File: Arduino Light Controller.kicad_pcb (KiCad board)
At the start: 2 copper layers, 100 x 75 mm, 61 parts, among them J1 61300311121, J10 61300211121, J11 61300211121, J12 61300411121, J13 61300211121, J14 61300211121, J15 61300211121, J16 61300411121, J17 61300211121, J18 61300211121, J19 61300211121, J2 61300211121, J20 61300411121, J21 61300211121, J22 61300311121, J23 61300211121, J24 61300211121, J25 61300211121, J26 61300211121, J27 61300211121, J28 61300211121, J29 61300211121, J3 61300211121, J30 61300211121, J31 61300211121, J32 61300211121, J33 61300211121, J34 61300211121, J35 61300211121, J36 61300211121, J37 61300211121, J38 61300211121, J4 61300211121, J5 61300211121, J6 61300211121, J7 61300211121, J8 61300411121, J9 61300211121

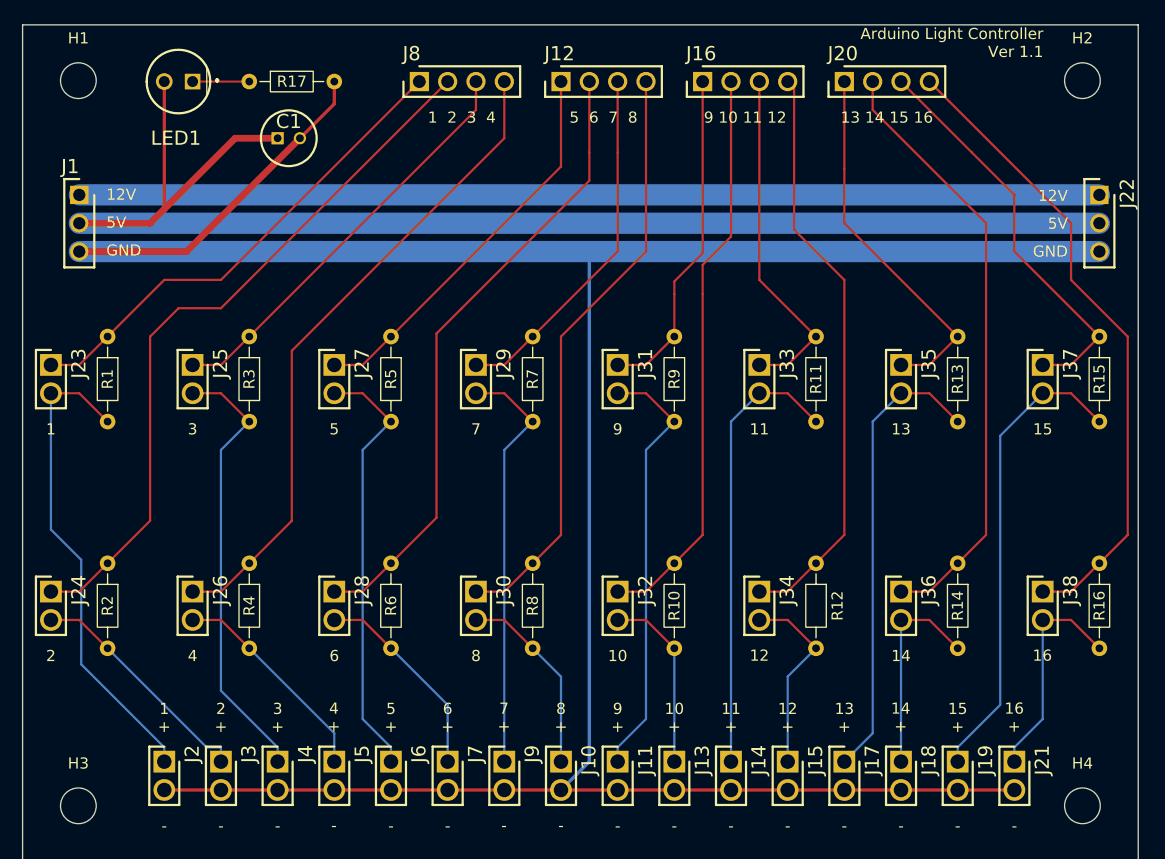
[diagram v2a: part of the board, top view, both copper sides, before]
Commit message: Updated components to the custom library and applied additional standards.
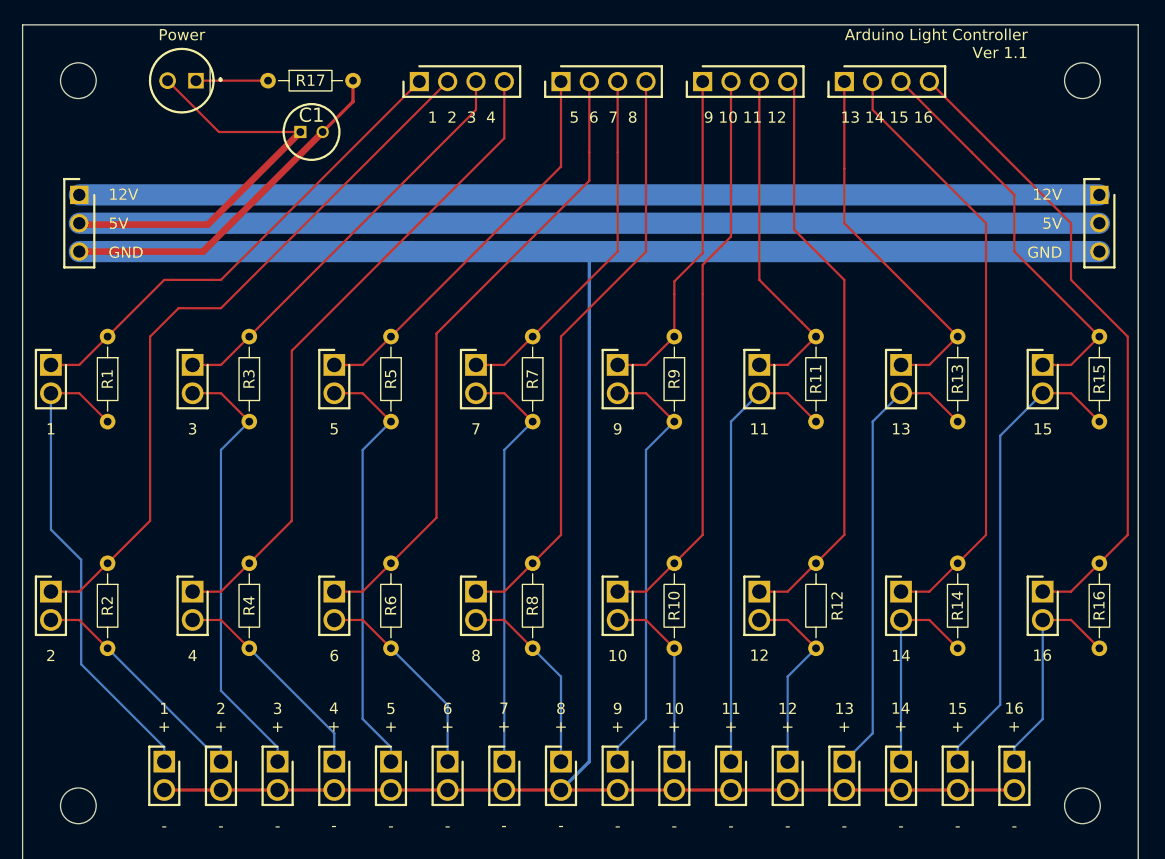
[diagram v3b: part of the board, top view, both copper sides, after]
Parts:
- moved C1 2.12 mm to (124.9, 59.6)
- moved R17 1.68 mm to (122.0, 55.0)
- moved LED1 0.31 mm to (115.5, 55.0)
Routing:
- net +5V: track 123.8 -> 128.6 mm
- net GND: track 247.3 -> 248.9 mm
- net Net-(LED1-K): track 5.08 -> 6.46 mm
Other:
- board text added: "Power"

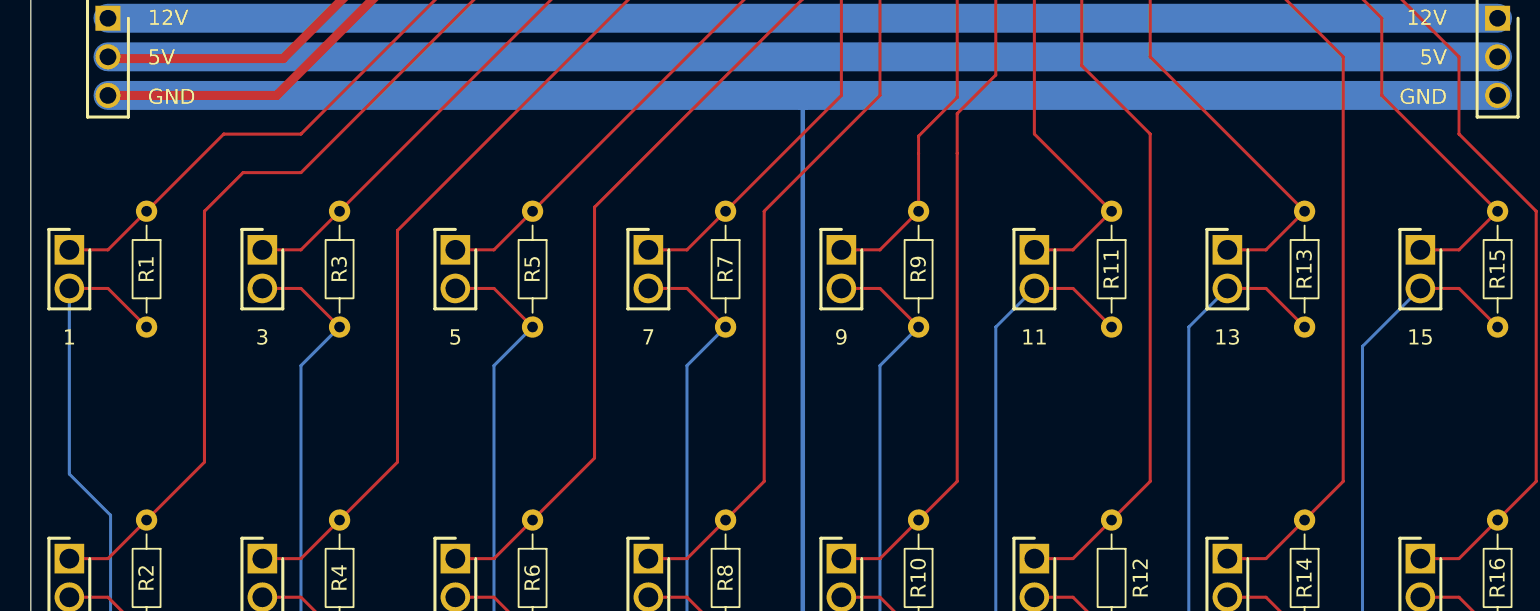
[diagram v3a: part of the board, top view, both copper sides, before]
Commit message: Added Resistor Bypass label to jumper pins.
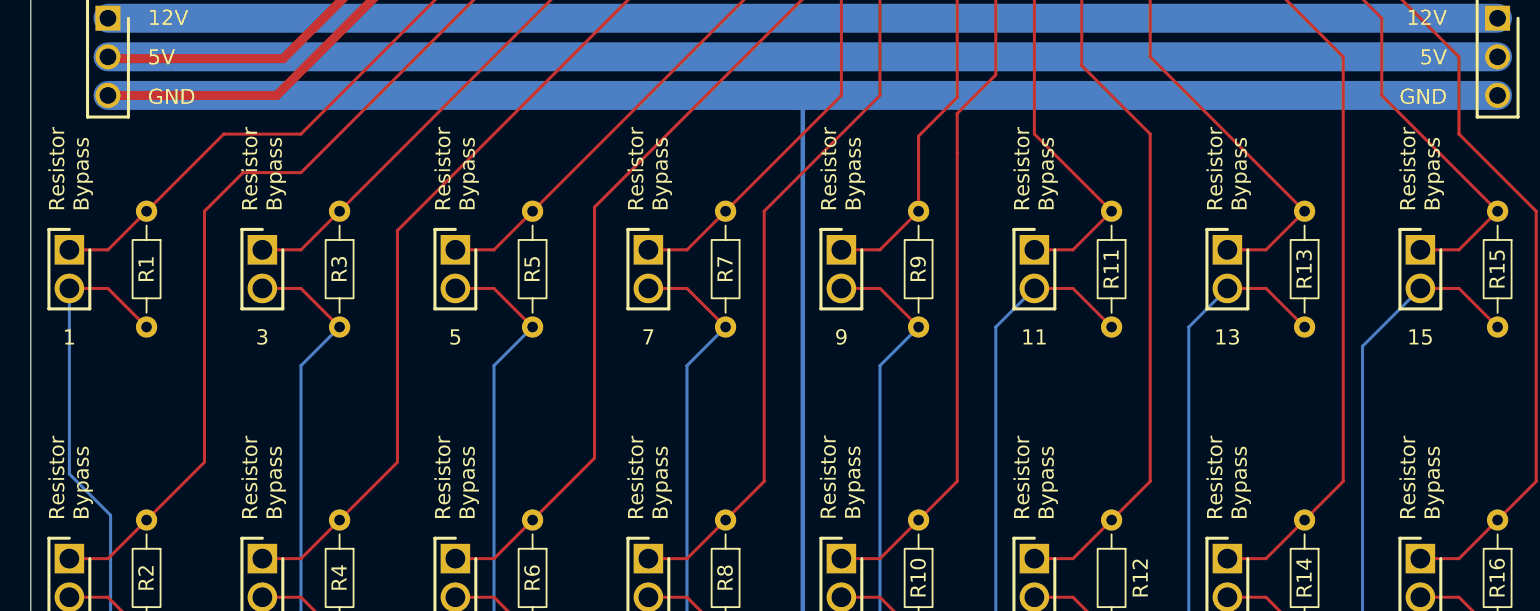
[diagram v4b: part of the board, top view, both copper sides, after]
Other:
- board text added: "Resistor Bypass"
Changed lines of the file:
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@@
+		)
+	)
+	(gr_text "Resistor\nBypass"
+		(at 178.74 77.94 90)
+		(layer "F.SilkS")
+		(effects
+			(font
+				(size 1 1)
+				(thickness 0.1)
+			)
+			(justify left)
 		)
 	)
@@
 		)
 	)
+	(gr_text "Resistor\nBypass"
+		(at 140.64 98.26 90)
+		(layer "F.SilkS")
+		(effects
+			(font
+				(size 1 1)
+				(thickness 0.1)
+			)
+			(justify left)
+		)
+	)
 	(gr_text "3\n+"
 		(at 122.86 113.5 0)
@@
 		)
 	)
+	(gr_text "Resistor\nBypass"
+		(at 115.24 77.94 90)
+		(layer "F.SilkS")
+		(effects
+			(font
+				(size 1 1)
+				(thickness 0.1)
+			)
+			(justify left)
+		)
+	)
 	(gr_text "6\n+"
 		(at 138.1 113.5 0)
@@
 		)
 	)
+	(gr_text "Resistor\nBypass"
+		(at 153.309206 98.243621 90)
+		(layer "F.SilkS")
+		(effects
+			(font
+				(size 1 1)
+				(thickness 0.1)
+			)
+			(justify left)
+		)
+	)
 	(gr_text "7\n+"
 		(at 143.150584 113.474628 0)
@@
 		)
 	)
+	(gr_text "Resistor\nBypass"
+		(at 191.44 77.94 90)
+		(layer "F.SilkS")
+		(effects
+			(font
+				(size 1 1)
+				(thickness 0.1)
+			)
+			(justify left)
+		)
+	)
 	(gr_text "7"
 		(at 140.64 86.83 0)
@@
 		)
 	)
+	(gr_text "Resistor\nBypass"
+		(at 153.34 77.94 90)
+		(layer "F.SilkS")
+		(effects
+			(font
+				(size 1 1)
+				(thickness 0.1)
+			)
+			(justify left)
+		)
+	)
 	(gr_text "11"
 		(at 166.04 86.83 0)
@@
 		)
 	)
+	(gr_text "Resistor\nBypass"
+		(at 178.74 98.26 90)
+		(layer "F.SilkS")
+		(effects
+			(font
+				(size 1 1)
+				(thickness 0.1)
+			)
+			(justify left)
+		)
+	)
+	(gr_text "Resistor\nBypass"
+		(at 102.54 77.94 90)
+		(layer "F.SilkS")
+		(effects
+			(font
+				(size 1 1)
+				(thickness 0.1)
+			)
+			(justify left)
+		)
+	)
+	(gr_text "Resistor\nBypass"
+		(at 127.94 77.94 90)
+		(layer "F.SilkS")
+		(effects
+			(font
+				(size 1 1)
+				(thickness 0.1)
+			)
+			(justify left)
+		)
+	)
 	(gr_text "4\n+"
 		(at 127.905646 113.474628 0)
@@
 		)
 	)
+	(gr_text "Resistor\nBypass"
+		(at 166.04 98.26 90)
+		(layer "F.SilkS")
+		(effects
+			(font
+				(size 1 1)
+				(thickness 0.1)
+			)
+			(justify left)
+		)
+	)
 	(gr_text "12V"
 		(at 193.2 65.8 0)
@@
 		)
 	)
+	(gr_text "Resistor\nBypass"
+		(at 127.94 98.26 90)
+		(layer "F.SilkS")
+		(effects
+			(font
+				(size 1 1)
+				(thickness 0.1)
+			)
+			(justify left)
+		)
+	)
 	(gr_text "-"
 		(at 133.02 122.39 0)
@@
 			)
 			(justify bottom)
+		)
+	)
+	(gr_text "Resistor\nBypass"
+		(at 140.64 77.94 90)
+		(layer "F.SilkS")
+		(effects
+			(font
+				(size 1 1)
+				(thickness 0.1)
+			)
+			(justify left)
+		)
+	)
+	(gr_text "Resistor\nBypass"
+		(at 115.24 98.26 90)
+		(layer "F.SilkS")
+		(effects
+			(font
+				(size 1 1)
+				(thickness 0.1)
+			)
+			(justify left)
 		)
 	)
@@
 		)
 	)
+	(gr_text "Resistor\nBypass"
+		(at 102.54 98.26 90)
+		(layer "F.SilkS")
+		(effects
+			(font
+				(size 1 1)
+				(thickness 0.1)
+			)
+			(justify left)
+		)
+	)
 	(gr_text "5V"
 		(at 193.2 68.4 0)
@@
 		)
 	)
+	(gr_text "Resistor\nBypass"
+		(at 191.44 98.26 90)
+		(layer "F.SilkS")
+		(effects
+			(font
+				(size 1 1)
+				(thickness 0.1)
+			)
+			(justify left)
+		)
+	)
+	(gr_text "Resistor\nBypass"
+		(at 166.04 77.94 90)
+		(layer "F.SilkS")
+		(effects
+			(font
+				(size 1 1)
+				(thickness 0.1)
+			)
+			(justify left)
+		)
+	)

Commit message: Updated sheets with title, version, and date.  Corrected issue with resistor placement and connection on PowerLED module.
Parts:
- J1, J22: value 61300311121 -> Header-1x3-TH; footprint SamacSys_Parts:HDRV3W64P0X254_1X3_762X254X869P -> Custom:710-61300311121
- J10, J11, J13, J14, J15, J17, J18, J19, J2, J21, J23, J24, J25, J26, J27, J28, J29, J3, J30, J31, J32, J33, J34, J35, J36, J37, J38, J4, J5, J6, J7, J9: value 61300211121 -> Header-1x2-TH; footprint SamacSys_Parts:HDRV2W110P0X254_1X2_508X254X854P -> Custom:710-61300211121
- J12, J16, J20, J8: value 61300411121 -> Header-1x4-TH; footprint SamacSys_Parts:HDRV4W95P0X254_1X4_1016X254X854P -> Custom:710-61300411121
- R1, R10, R11, R12, R13, R14, R15, R16, R17, R2, R3, R4, R5, R6, R7, R8, R9: value CFR-25JB-52-1K -> RES-1K-TH

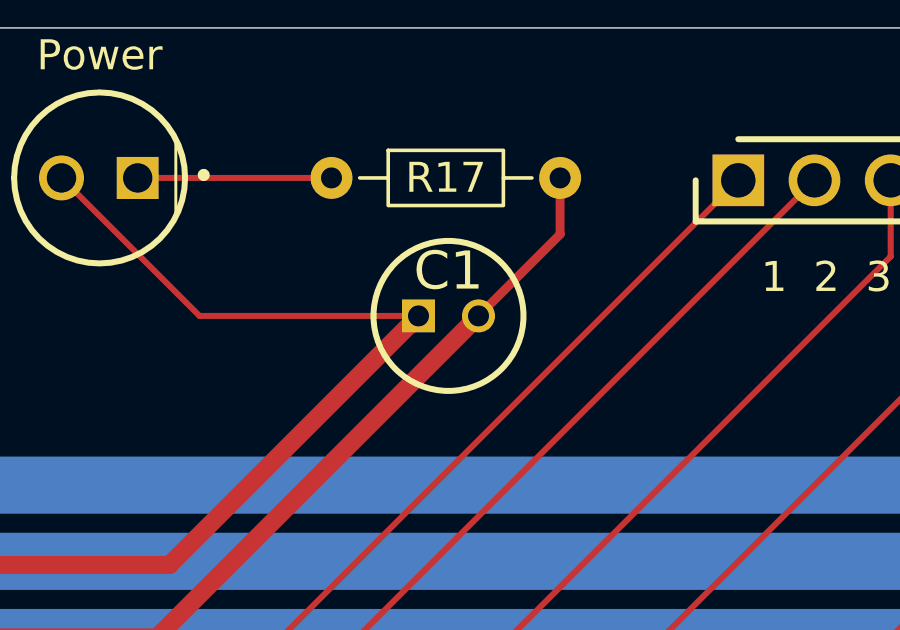
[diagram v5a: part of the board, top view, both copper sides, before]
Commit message: Missed updating PowerLED module with components from the custom library.
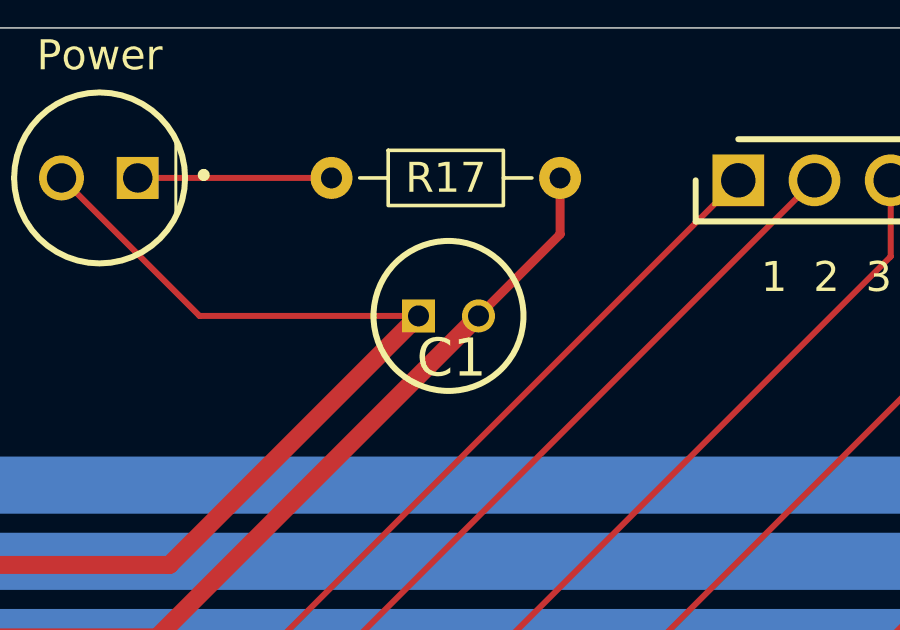
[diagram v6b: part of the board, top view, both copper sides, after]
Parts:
- C1: value 860010472002 -> CapE-10uf-25V-TH; footprint SamacSys_Parts:CAPPRD200W52D500H1250 -> Custom:710-860010472002
- LED1: value WP7113GD -> LED-Green-TH; footprint SamacSys_Parts:L53ND -> Custom:604-WP7113GD
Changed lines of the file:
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@@
 		)
 	)
-	(footprint "SamacSys_Parts:L53ND"
+	(footprint "Custom:604-WP7113GD"
 		(layer "F.Cu")
 		(at 115.54 55 180)
@@
 		(tags "LED")
 		(property "Reference" "LED1"
-			(at 1.5 -5.08 0)
+			(at 1.5 5 180)
 			(layer "F.SilkS")
 			(hide yes)
@@
 			)
 		)
-		(property "Value" "WP7113GD"
-			(at 1.27 0 0)
+		(property "Value" "LED-Green-TH"
+			(at 1.27 0 180)
 			(layer "F.SilkS")
 			(hide yes)
@@
 		)
 		(property "Datasheet" "https://www.kingbrightusa.com/images/catalog/SPEC/WP7113GD.pdf"
-			(at 0 0 0)
+			(at 0 0 180)
 			(layer "F.Fab")
 			(hide yes)
@@
 			)
 		)
-		(property "Description" "Standard LEDs - Through Hole GREEN DIFFUSED"
-			(at 0 0 0)
+		(property "Description" "LED - Through Hole GREEN DIFFUSED"
+			(at 0 0 180)
 			(layer "F.Fab")
 			(hide yes)
@@
 			)
 		)
+		(property "Supplier" "Mouser"
+			(at 0 0 180)
+			(unlocked yes)
+			(layer "F.Fab")
+			(hide yes)
+			(effects
+				(font
+					(size 1 1)
+					(thickness 0.15)
+				)
+			)
+		)
+		(property "Supplier Part Number" "604-WP7113GD"
+			(at 0 0 180)
+			(unlocked yes)
+			(layer "F.Fab")
+			(hide yes)
+			(effects
+				(font
+					(size 1 1)
+					(thickness 0.15)
+				)
+			)
+		)
+		(property "Supplier Price/Stock" "https://www.mouser.co.uk/ProductDetail/Kingbright/WP7113GD?qs=pz0eHrWKk7njL1kTYKysuw%3D%3D"
+			(at 0 0 180)
+			(unlocked yes)
+			(layer "F.Fab")
+			(hide yes)
+			(effects
+				(font
+					(size 1 1)
+					(thickness 0.15)
+				)
+			)
+		)
 		(sheetname "/PowerLED/")
 		(sheetfile "PowerLED.kicad_sch")
@@
 		)
 		(fp_text user "${REFERENCE}"
-			(at 1.27 -5.08 0)
+			(at 1.27 0 180)
 			(layer "F.Fab")
 			(effects
@@
 		)
 	)
-	(footprint "SamacSys_Parts:CAPPRD200W52D500H1250"
+	(footprint "Custom:710-860010472002"
 		(layer "F.Cu")
 		(at 124.9 59.6)
@@
 		(tags "Capacitor Polarised")
 		(property "Reference" "C1"
-			(at 1 -1.5 0)
+			(at 1.1 1.4 0)
 			(layer "F.SilkS")
 			(effects
@@
 			)
 		)
-		(property "Value" "860010472002"
+		(property "Value" "CapE-10uf-25V-TH"
 			(at 0 0 0)
 			(layer "F.SilkS")
@@
 			(at 0 0 0)
 			(unlocked yes)
+			(layer "F.Fab")
+			(hide yes)
+			(effects
+				(font
+					(size 1 1)
+					(thickness 0.15)
+				)
+			)
+		)
+		(property "Supplier" "Mouser"
+			(at 0 0 0)
+			(unlocked yes)
+			(layer "F.Fab")
+			(hide yes)
+			(effects
+				(font
+					(size 1 1)
+					(thickness 0.15)
+				)
+			)
+		)
+		(property "Supplier Part Number" "710-860010472002"
+			(at 0 0 0)
+			(unlocked yes)
+			(layer "F.Fab")
+			(hide yes)
+			(effects
+				(font
+					(size 1 1)
+					(thickness 0.15)
+				)
+			)
+		)
+		(property "Supplier Price/Stock" "https://www.mouser.co.uk/ProductDetail/Wurth-Elektronik/860010472002?qs=0KOYDY2FL2%2FyXlauDHcLjg%3D%3D"
+			(at 0 0 0)
+			(unlocked yes)
